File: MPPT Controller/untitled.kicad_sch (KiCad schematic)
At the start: 29 parts, among them J5 USB_C_Receptacle_USB2.0_16P, U2 ESP32-WROOM-32D, U3 CH340C

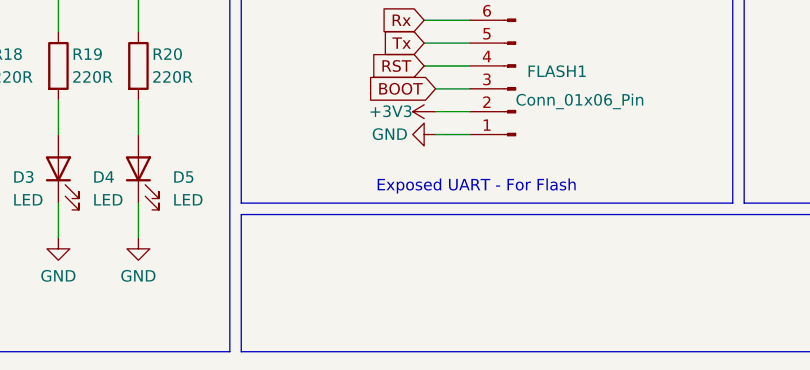
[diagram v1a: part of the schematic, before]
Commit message: Add I2C Pullup
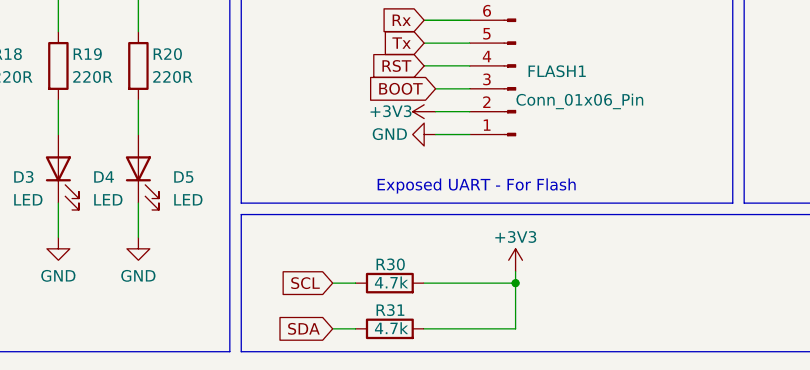
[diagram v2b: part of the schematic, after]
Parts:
- added R30, R31: 4.7k, Resistor_SMD:R_0603_1608Metric_Pad0.98x0.95mm_HandSolder, symbol Device:R
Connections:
- net +3V3: now also R30.2, R31.2
- net SCL: now also R30.1
- net SDA: now also R31.1

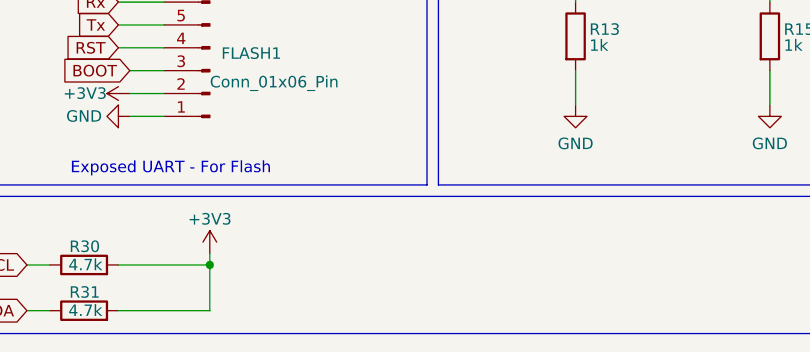
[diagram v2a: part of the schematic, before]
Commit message: Add Aux I2C Input
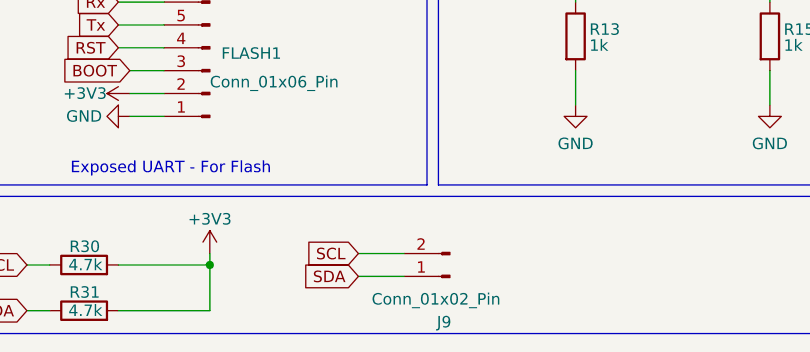
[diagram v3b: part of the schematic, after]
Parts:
- added J9: Conn_01x02_Pin, Connector_PinHeader_2.54mm:PinHeader_1x02_P2.54mm_Vertical, symbol Connector:Conn_01x02_Pin
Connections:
- net SCL: now also J9.2 (Pin_2)
- net SDA: now also J9.1 (Pin_1)
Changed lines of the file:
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@@
 	(wire
 		(pts
+			(xy 114.3 147.32) (xy 119.38 147.32)
+		)
+		(stroke
+			(width 0)
+			(type default)
+		)
+	)
+	(wire
+		(pts
 			(xy 55.88 139.7) (xy 55.88 143.51)
 		)
@@
 	(wire
 		(pts
+			(xy 114.3 149.86) (xy 119.38 149.86)
+		)
+		(stroke
+			(width 0)
+			(type default)
+		)
+	)
+	(wire
+		(pts
 			(xy 17.78 116.84) (xy 17.78 120.65)
 		)
@@
 		)
 	)
+	(global_label "SCL"
+		(shape input)
+		(at 114.3 147.32 180)
+		(fields_autoplaced yes)
+		(effects
+			(font
+				(size 1.27 1.27)
+			)
+			(justify right)
+		)
+		(property "Intersheetrefs" "${INTERSHEET_REFS}"
+			(at 107.8072 147.32 0)
+			(effects
+				(font
+					(size 1.27 1.27)
+				)
+				(justify right)
+				(hide yes)
+			)
+		)
+	)
 	(global_label "BOOT"
 		(shape input)
@@
 		)
 	)
+	(global_label "SDA"
+		(shape input)
+		(at 114.3 149.86 180)
+		(fields_autoplaced yes)
+		(effects
+			(font
+				(size 1.27 1.27)
+			)
+			(justify right)
+		)
+		(property "Intersheetrefs" "${INTERSHEET_REFS}"
+			(at 107.7467 149.86 0)
+			(effects
+				(font
+					(size 1.27 1.27)
+				)
+				(justify right)
+				(hide yes)
+			)
+		)
+	)
 	(global_label "D+"
 		(shape input)
@@
 					(unit 1)
 				)
+			)
+		)
+	)
+	(symbol
+		(lib_id "Connector:Conn_01x02_Pin")
+		(at 124.46 149.86 180)
+		(unit 1)
+		(exclude_from_sim no)
+		(in_bom yes)
+		(on_board yes)
+		(dnp no)
+		(property "Reference" "J9"
+			(at 123.825 154.94 0)
+			(effects
+				(font
+					(size 1.27 1.27)
+				)
+			)
+		)
+		(property "Value" "Conn_01x02_Pin"
+			(at 122.936 152.4 0)
+			(effects
+				(font
+					(size 1.27 1.27)
+				)
+			)
+		)
+		(property "Footprint" "Connector_PinHeader_2.54mm:PinHeader_1x02_P2.54mm_Vertical"
+			(at 124.46 149.86 0)
+			(effects
+				(font
+					(size 1.27 1.27)
+				)
+				(hide yes)
+			)
+		)
+		(property "Datasheet" "~"
+			(at 124.46 149.86 0)
+			(effects
+				(font
+					(size 1.27 1.27)
+				)
+				(hide yes)
+			)
+		)
+		(property "Description" "Generic connector, single row, 01x02, script generated"
+			(at 124.46 149.86 0)
+			(effects
+				(font
+					(size 1.27 1.27)
+				)
+				(hide yes)
+			)
+		)
+		(pin "1"
+		)
+		(pin "2"
+		)
+		(instances
+			(project "MPPT-Controller"
+				(path "/3478fe58-6c48-40fd-90f3-a0feb3af5722/0f80c830-9625-4e30-9255-a3bc6189ae7c"
+					(reference "J9")
+					(unit 1)
+				)
